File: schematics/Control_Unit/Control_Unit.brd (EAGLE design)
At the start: 58.4 x 86.3 mm, 165 parts, among them IC1 74HC174N, IC10 74HC74N, IC100 74HCT32N, IC101 74HCT08N, IC102 74HC151N, IC103 74HC373N, IC104 74HCT08N, IC105 74HC151N, IC106 74HC151N, IC107 74HCT04N, IC108 74HCT32N, IC109 74HCT08N, IC11 74HC74N, IC110 74HCT32N, IC111 74HC151N, IC112 74HCT32N, IC113 74HC151N, IC114 74HC151N, IC115 74HC151N, IC116 74HC373N, IC117 74HC74N, IC12 74AC08N, IC124 74HCT32N, IC125 74HCT08N, IC126 74AC157N, IC127 74HCT08N, IC128 74AC08N, IC129 74AC08N, IC13 74AC08N, IC130 74HCT04N, IC133 74HCT04N, IC134 74HCT08N, IC135 74HCT08N, IC136 74HCT08N, IC14 74HC74N, IC141 74HCT32N, IC15 74HC74N, IC16 74AC08N, IC164 74HC174N, IC165 74HC174N, IC166 74HC174N, IC167 74HC174N, IC168 74HCT32N, IC169 74HCT32N, IC17 74HCT32N, IC172 74HCT32N, IC173 74HCT32N, IC175 74HC193N, IC176 74HC193N, IC177 74HC193N, IC178 74HC193N, IC179 74HC193N, IC18 74AC08N, IC180 74HC193N, IC181 74HC193N, IC182 74HC193N, IC19 74AC08N, IC190 74HCT32N, IC191 74HCT32N, IC2 74HC174N, IC20 74AC08N, IC21 74AC08N, IC22 74HCT32N, IC23 74HCT08N, IC24 74HCT08N, IC25 74HCT32N, IC26 74HCT08N, IC27 74HCT08N, IC28 74HCT08N, IC29 74HCT32N, IC3 74HC151N, IC30 74HCT08N, IC32 74HCT32N, IC33 74HCT32N, IC34 74HCT08N, IC35 74HCT04N, IC36 CY62256LL-PC, IC37 74HCT04N, IC38 74HCT08N, IC39 74HCT08N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

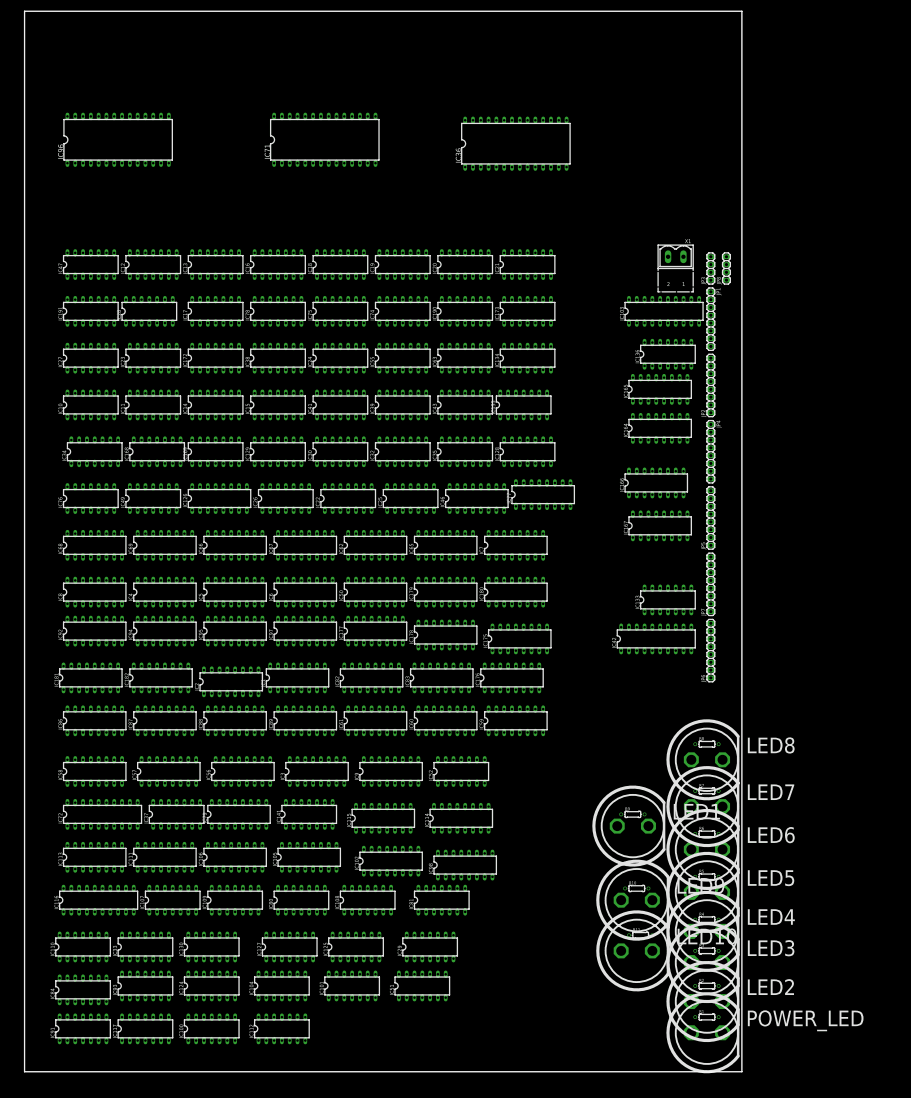
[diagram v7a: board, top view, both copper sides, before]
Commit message: add proper connectors
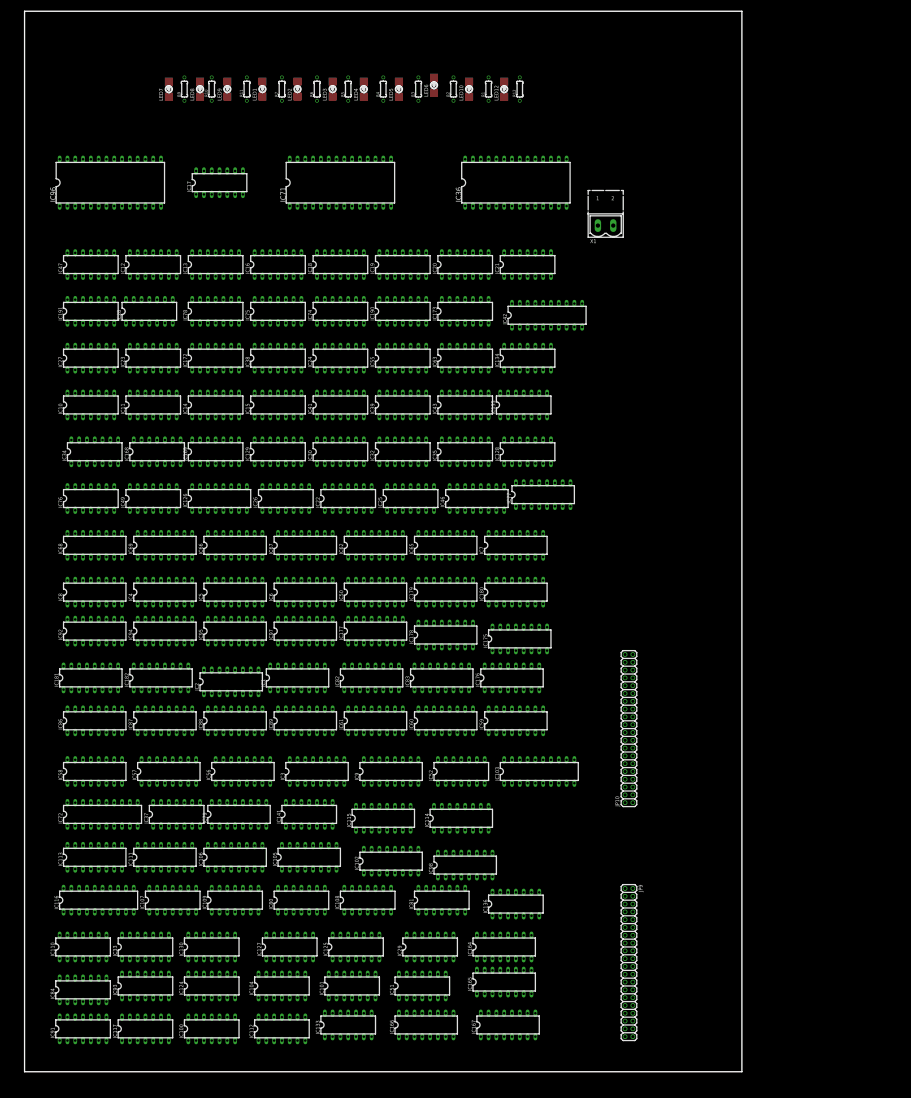
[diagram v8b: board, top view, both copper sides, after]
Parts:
- removed JP1, JP2, JP4, JP5, JP6, JP7: (no value), pinhead:1X08
- removed JP3, JP8: (no value), pinhead:1X04
- removed POWER_LED: (no value), led:LED5MM
- removed R8: (no value), resistor:0204/7
- added JP10, JP9: (no value), pinhead:2X20
- added LED12: P4-TOP, led:P47F-TOP
- added R12: (no value), resistor:0204/7
- LED1, LED10, LED2, LED3, LED4, LED5, LED6, LED7, LED8, LED9: value (none) -> P4-TOP; device led:LED5MM -> led:P47F-TOP
- moved LED2 81.4 mm to (22.5, 80.0), turned to 90 degrees
- moved R1 77.6 mm to (38.1, 80.0), turned to 90 degrees
- moved LED3 77.4 mm to (25.4, 80.0), turned to 90 degrees
- moved R11 76.0 mm to (18.4, 80.0), turned to 90 degrees
- moved R2 75.9 mm to (35.2, 80.0), turned to 90 degrees
- moved LED4 74.1 mm to (27.9, 80.0), turned to 90 degrees
- moved R3 74.0 mm to (32.4, 80.0), turned to 90 degrees
- moved LED9 74.0 mm to (16.8, 80.0), turned to 90 degrees
- moved R10 73.7 mm to (15.6, 80.0), turned to 90 degrees
- moved LED7 73.0 mm to (12.1, 80.0), turned to 90 degrees
- moved R4 72.6 mm to (29.5, 80.0), turned to 90 degrees
- moved LED10 71.5 mm to (36.5, 80.0), turned to 90 degrees
- moved R5 70.5 mm to (26.7, 80.0), turned to 90 degrees
- moved LED5 70.0 mm to (30.8, 80.0), turned to 90 degrees
- moved R9 69.4 mm to (13.3, 80.0), turned to 90 degrees
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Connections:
- removed net CYCL_0: IC10.12, IC10.5, IC80.5
- removed net N$169: LED6.A
- removed net N$173: LED2.A
- removed net N$176: LED3.A
- removed net N$179: LED4.A
- removed net N$182: LED5.A
- removed net N$188: LED7.A
- removed net N$189: LED8.K, R8.2
- removed net N$191: LED8.A
- removed net N$195: LED9.A
- removed net N$225: LED10.A
- removed net N$67: IC42.18, JP6.1
- removed net OPCODE_LOAD_INPUT: IC10.9, IC11.2, IC50.9, IC6.9, IC80.4
- removed net PC_COUNT_UP_FETCH2: IC124.2, IC14.12, IC14.5
- removed net STATE_0: IC101.9, IC14.9, IC15.2, IC23.1, IC23.12, IC24.12, IC27.9, IC28.1, IC38.9, IC51.4, IC74.1, IC74.9, IC78.12, IC81.12
- removed net STATE_1: IC104.12, IC15.12, IC15.5, IC23.4, IC24.1, IC26.1, IC27.1, IC27.12, IC38.1, IC51.1, IC74.12, IC74.4, IC75.1, IC81.9
- removed net STATE_2: IC104.1, IC117.2, IC15.9, IC23.9, IC24.4, IC26.4, IC27.4, IC28.9, IC38.4, IC51.9, IC75.4, IC81.4
- removed net STATE_3: IC104.9, IC117.12, IC117.5, IC24.9, IC26.9, IC28.12, IC38.12, IC51.12, IC75.12, IC81.1
- removed net STATE_4: IC10.2, IC101.1, IC117.9, IC127.4
- new net CYCL_1: IC10.12, IC10.5, IC80.5, LED1.A
- new net N$228: IC42.18, JP9.16
- new net OPCODE_LOAD_INPUT/CYCL_2: IC10.9, IC11.2, IC50.9, IC6.9, IC80.4, LED2.A
- new net PC_COUNT_UP_FETCH2/CYCL_5: IC124.2, IC14.12, IC14.5, LED5.A
- new net STATE_0/CYCL_6: IC101.9, IC14.9, IC15.2, IC23.1, IC23.12, IC24.12, IC27.9, IC28.1, IC38.9, IC51.4, IC74.1, IC74.9, IC78.12, IC81.12, LED6.A
- new net STATE_1/CYCL_7: IC104.12, IC15.12, IC15.5, IC23.4, IC24.1, IC26.1, IC27.1, IC27.12, IC38.1, IC51.1, IC74.12, IC74.4, IC75.1, IC81.9, LED7.A
- new net STATE_2/CYCL_8: IC104.1, IC117.2, IC15.9, IC23.9, IC24.4, IC26.4, IC27.4, IC28.9, IC38.4, IC51.9, IC75.4, IC81.4, LED8.A
- new net STATE_3/CYCL_9: IC104.9, IC117.12, IC117.5, IC24.9, IC26.9, IC28.12, IC38.12, IC51.12, IC75.12, IC81.1, LED9.A
- new net STATE_4/CYCL_10: IC10.2, IC101.1, IC117.9, IC127.4, LED12.A
- net ALU_CARRY_OUT: now also JP9.32; no longer JP8.4
- net ALU_NR3_ENABLE: now also JP9.26; no longer JP3.3
- net ALU_NR4_ENABLE: now also JP9.24; no longer JP3.4
- net CYCL_3: now also LED3.A
- net CYCL_4: now also LED4.A
- net DATA0: now also JP9.23; no longer JP4.1
- net DATA1: now also JP9.25; no longer JP4.2
- net DATA2: now also JP9.27; no longer JP4.3
- net DATA3: now also JP9.29; no longer JP4.4
- net DATA4: now also JP9.31; no longer JP4.5
- net DATA5: now also JP9.33; no longer JP4.6
- net DATA6: now also JP9.35; no longer JP4.7
- net DATA7: now also JP9.37; no longer JP4.8
- net DATA_BUS_ENABLE_LATCH: now also IC107.3; no longer IC35.9
- net GND: now also JP10.17, JP10.18, JP10.21, JP10.22, JP10.39, JP10.40, JP9.17, JP9.18, JP9.21, JP9.22, JP9.39, JP9.40, R12.1; no longer R8.1
- net IO_INPUT_0: now also JP10.2; no longer JP7.8
- net IO_INPUT_1: now also JP10.4; no longer JP7.7
- net IO_INPUT_2: now also JP10.6; no longer JP7.6
- net IO_INPUT_3: now also JP10.8; no longer JP7.5
- net IO_INPUT_4: now also JP10.10; no longer JP7.4
- net IO_INPUT_5: now also JP10.12; no longer JP7.3
- net IO_INPUT_6: now also JP10.14; no longer JP7.2
- net IO_INPUT_7: now also JP10.16; no longer JP7.1
- net LATCH_ALU_INPUT_B_JMP_O: now also IC63.12; no longer IC17.9
- net MEM_NOT_CE: now also IC17.8; no longer IC63.11
- net N$101: now also LED8.C; no longer LED9.K
- net N$109: now also IC63.13; no longer IC17.10
- net N$115: now also LED7.C; no longer LED1.K
- net N$119: now also JP9.1; no longer JP1.1
- net N$120: now also JP9.3; no longer JP1.2
- net N$126: now also IC17.9; no longer IC63.12
- net N$148: now also JP9.28; no longer JP3.2
- net N$165: now also LED10.C; no longer POWER_LED.K
- net N$168: now also LED12.C, R12.2; no longer LED1.A
- net N$170: now also JP9.5; no longer JP1.3
- net N$171: now also LED6.C; no longer LED2.K
- net N$172: now also JP9.7; no longer JP1.4
- net N$174: now also LED5.C; no longer LED3.K
- net N$175: now also JP9.9; no longer JP1.5
- net N$177: now also LED4.C; no longer LED4.K
- net N$178: now also JP9.11; no longer JP1.6
- net N$180: now also LED3.C; no longer LED5.K
- net N$181: now also JP9.13; no longer JP1.7
- net N$183: now also LED2.C; no longer LED6.K
- net N$184: now also JP9.15; no longer JP1.8
- net N$186: now also LED1.C; no longer LED7.K
- net N$200: now also IC17.10; no longer IC63.13
- net N$202: now also JP9.30; no longer JP3.1
- net N$32: now also JP10.1; no longer JP2.1
- net N$33: now also JP10.3; no longer JP2.2
- net N$44: now also JP10.5; no longer JP2.3
- net N$52: now also JP10.11; no longer JP2.6
- net N$58: now also IC42.7, JP9.6; no longer IC42.3, JP6.8
- net N$59: now also JP9.4; no longer JP6.7
- net N$60: now also IC42.3, JP9.2; no longer IC42.7, JP6.6
- net N$61: now also IC42.17, JP9.14; no longer IC42.8, JP6.5
- net N$62: now also IC42.14, JP9.12; no longer IC42.13, JP6.4
- net N$63: now also IC42.13, JP9.10; no longer IC42.14, JP6.3
- net N$66: now also IC42.8, JP9.8; no longer IC42.17, JP6.2
- net N$70: now also IC35.9; no longer IC107.3
- net N$74: now also JP10.7; no longer JP2.4
- net N$77: now also JP10.13; no longer JP2.7
- net N$79: now also JP10.15; no longer JP2.8
- net N$80: now also JP10.23; no longer JP5.1
- net N$81: now also JP10.25; no longer JP5.2
- net N$83: now also JP10.27; no longer JP5.3
- net N$88: now also JP10.29; no longer JP5.4
- net N$89: now also JP10.31; no longer JP5.5
- net N$91: now also JP10.33; no longer JP5.6
- net N$92: now also JP10.35; no longer JP5.7
- net N$93: now also JP10.37; no longer JP5.8
- net N$94: now also LED9.C; no longer LED10.K
- net N$95: now also JP10.9; no longer JP2.5
- net N$99: now also IC35.8; no longer IC107.4
- net REGS_OUTPUT_TO_DATABUS_ENABLE: now also IC107.4; no longer IC35.8
- net VCC: now also LED10.A; no longer POWER_LED.A
- net WRITE_PC_L_ALU_LATCH_JMP_O: now also IC63.11; no longer IC17.8
